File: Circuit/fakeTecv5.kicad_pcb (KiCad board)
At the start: 2 copper layers, 25.4 x 52.1 mm, 78 parts, among them J1 EXTRA, J11 FET1 3,3, J12 FET2 3,3, J13 FET3 3,3, J14 GPS Pins, J16 Encoder Pads, J37 SCL, J38 JST-SH-4, J39 SDA, J40 3.3V, J41 GND, J42 FET1, J43 FET2, J44 FET3, J45 GND, J46 3.3V, J47 GND, J48 GND, J49 GND, J5 I2C Oled screen, J50 3.3V, J51 GND, J52 GND, J6 FET1 Drain, J7 FET2 Drain, J8 FET3 Drain, J9 JST-PH-2, Q1 AO3400A, Q2 AO3400A, Q3 AO3400A, SW1 Reset, SW2 SW_Push, U1 XB8089D0, U2 HT-RA62, U3 nice!nano v2

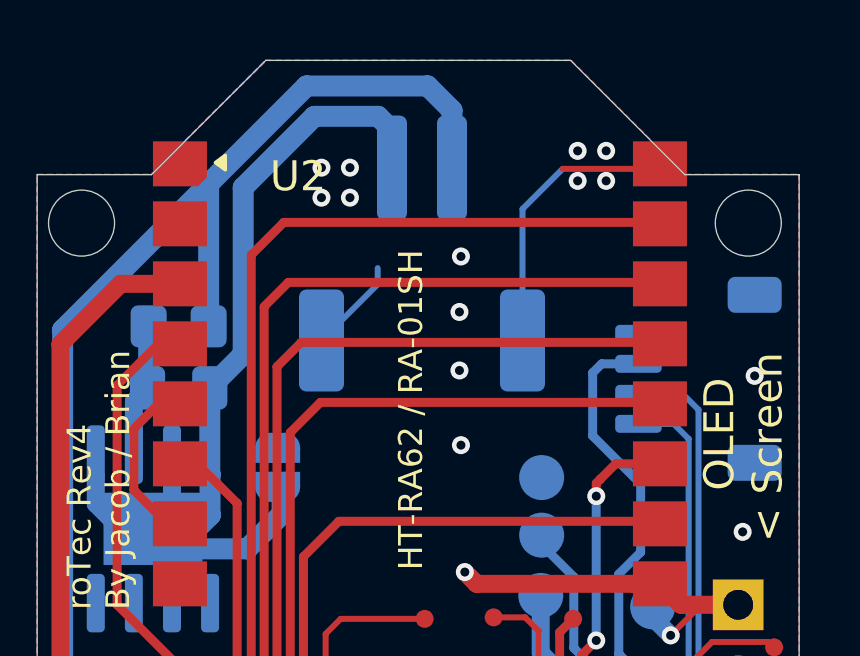
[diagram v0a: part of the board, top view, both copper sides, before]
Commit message: hw: modify power connector to support both JST GH and PH connector
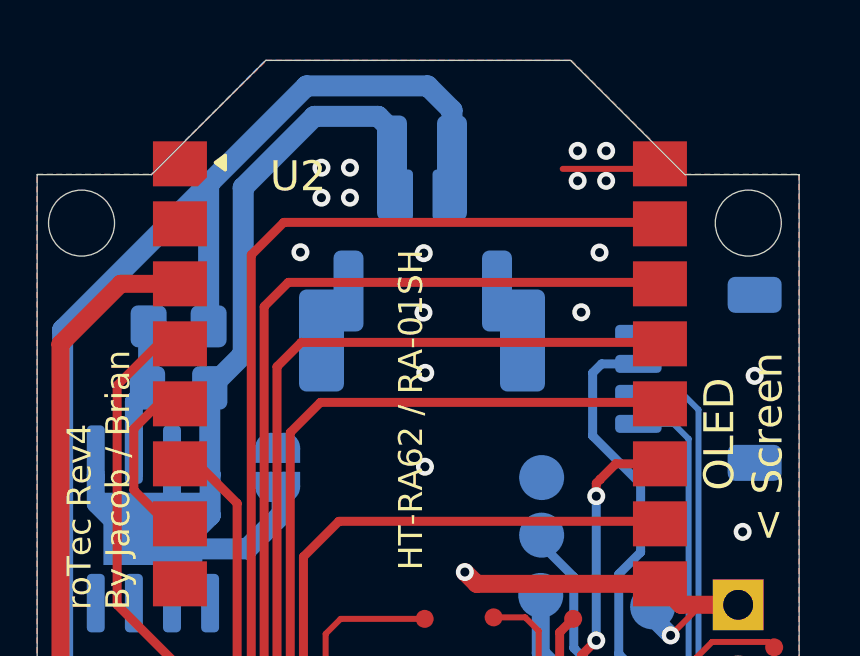
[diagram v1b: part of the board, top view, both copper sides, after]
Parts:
- J9: footprint Connector_JST:JST_PH_S2B-PH-SM4-TB_1x02-1MP_P2.00mm_Horizontal -> faketec:JST_PH_S2B-PH-SM4-TB_1x02-1MP_P2.00mm_Horizontal
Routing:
- net GND: track 133.1 -> 123.7 mm, vias 58 -> 61

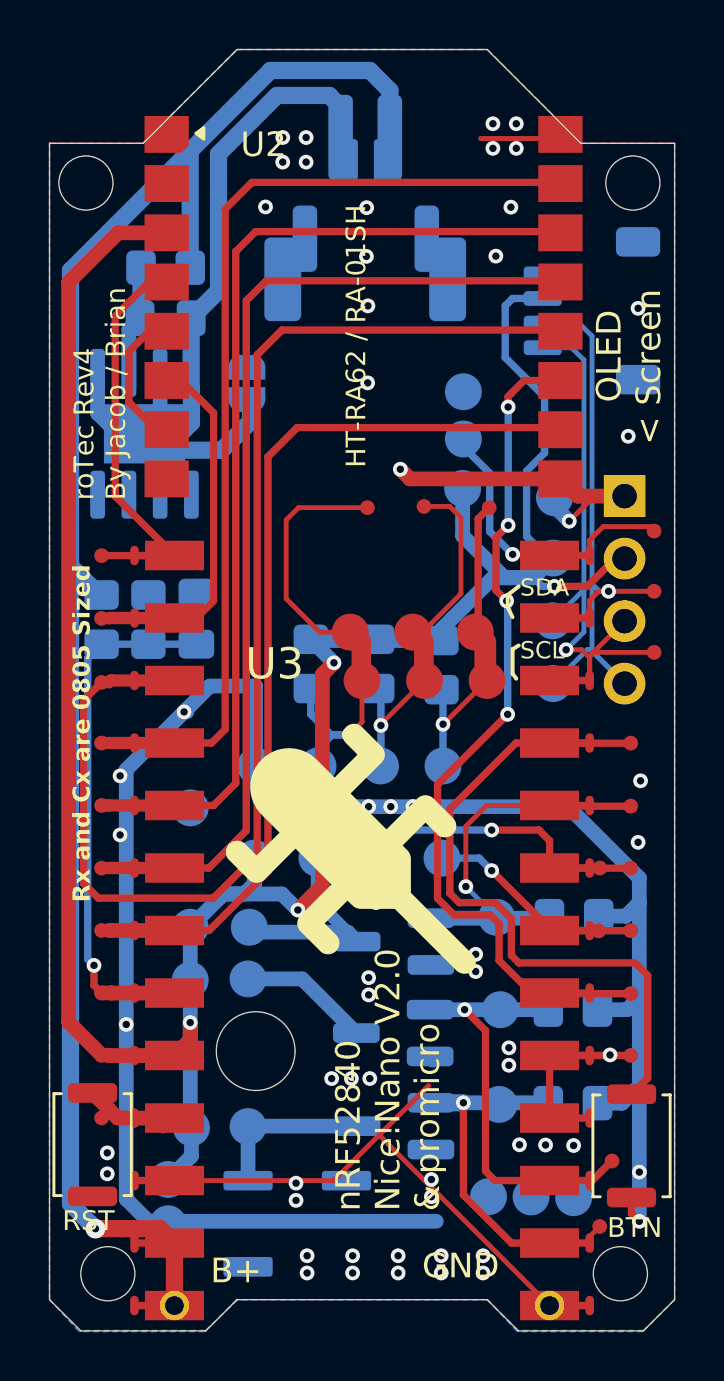
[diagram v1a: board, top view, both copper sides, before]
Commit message: hw: refactor spi routing. Make OLED screen pins friction fit
SPI is likely running under 50mHz mark so vias is not an issue and want to keep signal path small. Made careful note to keep all spi lines under the ground plane as much as possible.
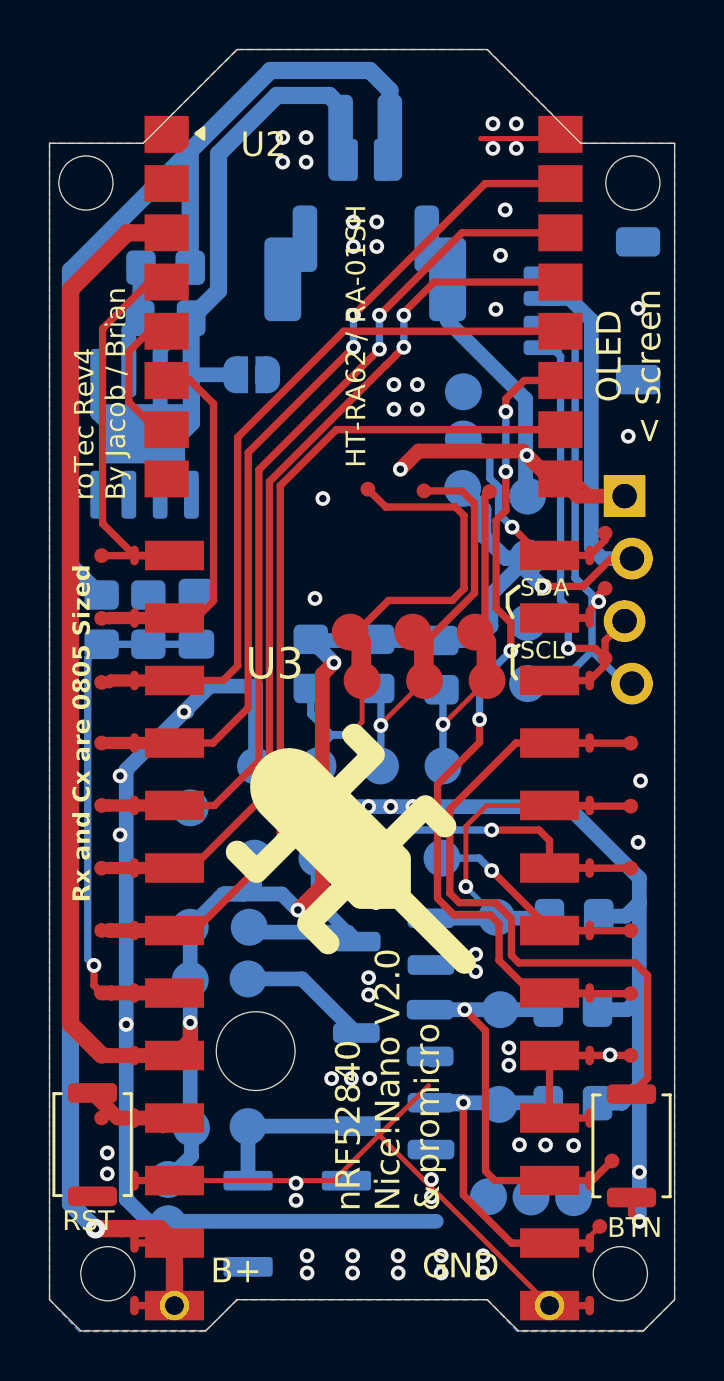
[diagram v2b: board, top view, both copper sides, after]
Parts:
- J5: footprint faketec:OLED_PinHeader_1x04_P2.54mm_Vertical -> faketec:OLED_PinHeader_1x04_P2.54mm_Vertical_Friction_Fit
- moved J25 2.00 mm to (121.5, 51.7)
- moved J24 1.99 mm to (121.5, 48.9)
- moved J23 1.99 mm to (121.5, 46.6)
- moved J41 1.09 mm to (118.3, 45.1)
- moved J3 0.75 mm to (111.8, 44.9)
- moved J22 0.65 mm to (116.8, 45.0)
- moved J2 0.63 mm to (114.1, 44.9)
- moved J37 0.58 mm to (118.8, 50.3)
- moved J40 0.54 mm to (118.8, 47.6)
- moved JP1 0.40 mm to (107.1, 40.2), turned to 180 degrees
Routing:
- net /SCK: track 52.5 -> 29.9 mm
- net GND: track 123.7 -> 132.5 mm, vias 61 -> 67
- net /CS: track 40.8 -> 34.7 mm, vias 0 -> 2
- net /MOSI: track 40.7 -> 35.8 mm, vias 0 -> 2
- net /MISO: track 40.8 -> 36.4 mm, vias 0 -> 2
- net /SCL: track 23.5 -> 19.4 mm
- net /ENC_PUSH: track 17.4 -> 20.9 mm
- net /SDA: track 27.3 -> 25.3 mm
- net /EXTRA: track 9.34 -> 7.40 mm
- net /ENC_A: track 14.9 -> 13.4 mm
- net /RST: track 16.3 -> 17.7 mm
- net -BATT: track 34.2 -> 32.9 mm
- net /BUSY: track 36.6 -> 35.3 mm

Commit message: hw: Thicker lines. All 0.2 lines converted to 0.3mm
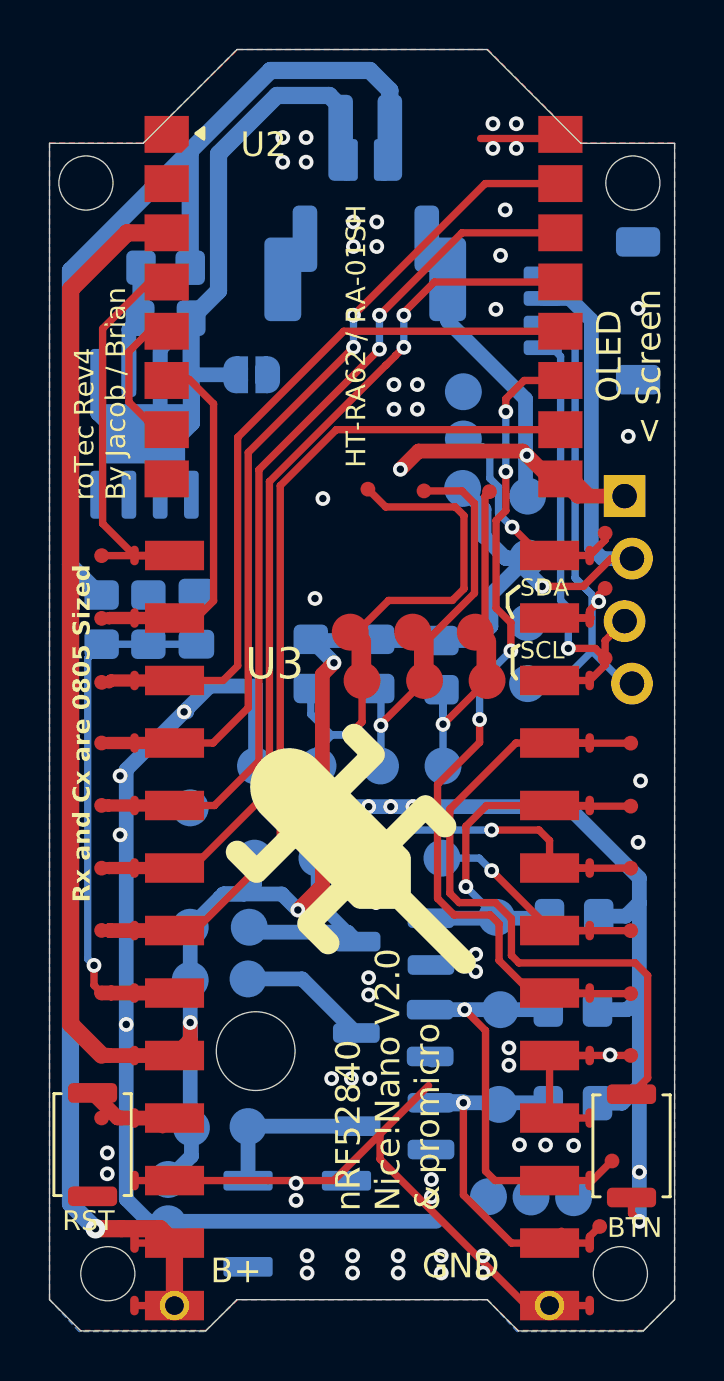
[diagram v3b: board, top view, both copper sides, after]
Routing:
- net GND: track 132.5 -> 133.1 mm
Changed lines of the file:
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@@
 		(start 103.65195 65.32401)
 		(end 103.96298 65.01298)
-		(width 0.2)
+		(width 0.3)
 		(layer "F.Cu")
 		(net 1)
@@
 		(start 103.96298 65.01298)
 		(end 103.96298 65.32401)
-		(width 0.2)
+		(width 0.3)
 		(layer "F.Cu")
 		(net 1)
@@
 	)
 	(segment
+		(start 119.20298 78.02401)
+		(end 118.26401 78.02401)
+		(width 0.3)
+		(layer "F.Cu")
+		(net 2)
+	)
+	(segment
 		(start 118.11 43.3)
 		(end 118.28 43.47)
@@
 		(start 121.01899 45.13101)
 		(end 122.25098 45.13101)
-		(width 0.2)
+		(width 0.3)
+		(layer "F.Cu")
+		(net 2)
+	)
+	(segment
+		(start 112.313 72.073)
+		(end 112.313 71.063)
+		(width 0.3)
 		(layer "F.Cu")
 		(net 2)
@@
 		(start 119.429058 30.6)
 		(end 116.4 30.6)
-		(width 0.2)
+		(width 0.3)
 		(layer "F.Cu")
 		(net 2)
@@
 		(start 107.75 72.94401)
 		(end 110.43199 72.94401)
-		(width 0.2)
+		(width 0.3)
+		(layer "F.Cu")
+		(net 2)
+	)
+	(segment
+		(start 118.26401 78.02401)
+		(end 112.313 72.073)
+		(width 0.3)
 		(layer "F.Cu")
 		(net 2)
@@
 	)
 	(segment
-		(start 112.313 71.13403)
-		(end 112.313 71.063)
-		(width 0.2)
-		(layer "F.Cu")
-		(net 2)
-	)
-	(segment
 		(start 119.41 67.86)
 		(end 122.51 67.86)
@@
 		(start 110.43199 72.94401)
 		(end 112.313 71.063)
-		(width 0.2)
+		(width 0.3)
 		(layer "F.Cu")
 		(net 2)
@@
 		(start 119.452024 30.622966)
 		(end 119.429058 30.6)
-		(width 0.2)
+		(width 0.3)
 		(layer "F.Cu")
 		(net 2)
@@
 		(start 103.96298 72.94401)
 		(end 107.75 72.94401)
-		(width 0.2)
+		(width 0.3)
 		(layer "F.Cu")
 		(net 2)
@@
 		(start 119.92798 44.04)
 		(end 121.01899 45.13101)
-		(width 0.2)
+		(width 0.3)
 		(layer "F.Cu")
 		(net 2)
@@
 		(start 112.313 71.063)
 		(end 114.288 69.088)
-		(width 0.2)
+		(width 0.3)
 		(layer "F.Cu")
 		(net 2)
@@
 	)
 	(segment
-		(start 119.20298 78.02401)
-		(end 112.313 71.13403)
-		(width 0.2)
-		(layer "F.Cu")
-		(net 2)
-	)
-	(segment
 		(start 122.25098 45.13101)
 		(end 120.34201 45.13101)
@@
 		(start 116.64599 57.70401)
 		(end 119.20298 57.70401)
-		(width 0.2)
+		(width 0.3)
 		(layer "F.Cu")
 		(net 17)
@@
 		(start 115.801 58.549)
 		(end 116.64599 57.70401)
-		(width 0.2)
+		(width 0.3)
 		(layer "F.Cu")
 		(net 17)
@@
 		(start 115.801 61)
 		(end 115.801 58.549)
-		(width 0.2)
+		(width 0.3)
 		(layer "F.Cu")
 		(net 17)
@@
 		(start 115.801 61)
 		(end 115.801 61.001)
-		(width 0.2)
+		(width 0.3)
 		(layer "B.Cu")
 		(net 17)
@@
 		(start 115.801 61.001)
 		(end 117.05 62.25)
-		(width 0.2)
+		(width 0.3)
 		(layer "B.Cu")
 		(net 17)
@@
 		(start 120.83298 75.21702)
 		(end 121.24 74.81)
-		(width 0.2)
+		(width 0.3)
 		(layer "F.Cu")
 		(net 21)
@@
 		(start 119.68699 75)
 		(end 119.20298 75.48401)
-		(width 0.2)
+		(width 0.3)
 		(layer "F.Cu")
 		(net 21)
@@
 		(start 120.83298 75.48401)
 		(end 120.83298 75.21702)
-		(width 0.2)
+		(width 0.3)
 		(layer "F.Cu")
 		(net 21)
@@
 		(start 120.89599 50.08401)
 		(end 120.83298 50.08401)
-		(width 0.2)
+		(width 0.3)
 		(layer "F.Cu")
 		(net 22)
@@
 		(start 122.25098 52.75101)
 		(end 122.65098 52.75101)
-		(width 0.2)
+		(width 0.3)
 		(layer "B.Cu")
 		(net 22)
@@
 		(start 119.283 60.16068)
 		(end 119.19967 60.24401)
-		(width 0.2)
+		(width 0.3)
 		(layer "F.Cu")
 		(net 24)
@@
 		(start 116.66298 52.62401)
 		(end 114.88699 54.4)
-		(width 0.2)
+		(width 0.3)
 		(layer "F.Cu")
 		(net 30)
@@
 		(start 114.88699 54.4)
 		(end 114.873 54.4)
-		(width 0.2)
+		(width 0.3)
 		(layer "F.Cu")
 		(net 30)
@@
 		(start 114.873 52.6)
 		(end 114.873 54.4)
-		(width 0.2)
+		(width 0.3)
 		(layer "B.Cu")
 		(net 30)
@@
 		(start 112.35 54.39699)
 		(end 114.12298 52.62401)
-		(width 0.2)
+		(width 0.3)
 		(layer "F.Cu")
 		(net 31)
@@
 		(start 112.35 54.45)
 		(end 112.35 54.39699)
-		(width 0.2)
+		(width 0.3)
 		(layer "F.Cu")
 		(net 31)
@@
 		(start 111.58298 54.30702)
 		(end 111.063 54.827)
-		(width 0.2)
+		(width 0.3)
 		(layer "F.Cu")
 		(net 32)
@@
 		(start 111.58298 52.62401)
 		(end 111.58298 54.30702)
-		(width 0.2)
+		(width 0.3)
 		(layer "F.Cu")
 		(net 32)
@@
 		(start 121.05 47.32699)
 		(end 120.83298 47.54401)
-		(width 0.2)
+		(width 0.3)
 		(layer "F.Cu")
 		(net 33)

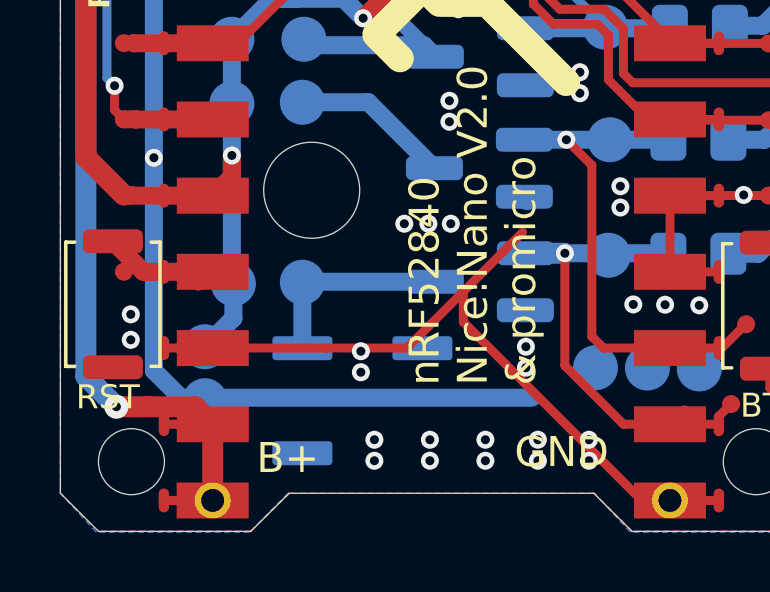
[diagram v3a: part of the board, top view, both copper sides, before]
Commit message: hw: Buzzer is wired incorrectly. Fixed wiring and updated schematic and pcb
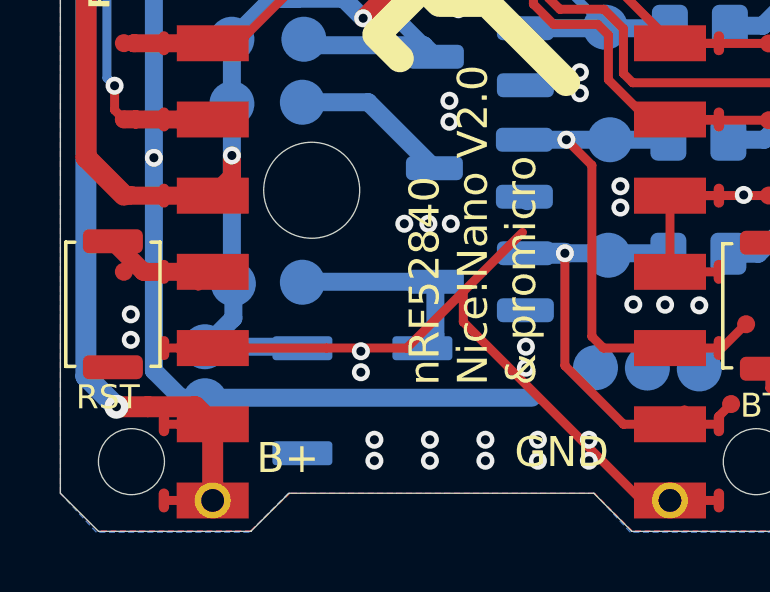
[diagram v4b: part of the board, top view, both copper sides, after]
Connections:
- BZ1 pad 1: /BUZZER -> +3.3V
- BZ1 pad 2: GND -> /BUZZER
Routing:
- net +3.3V: track 108.3 -> 111.6 mm
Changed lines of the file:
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@@
 			(layers "F.Cu" "F.Mask" "F.Paste")
 			(net 30 "/ENC_A")
-			(pinfunction "P1.07")
+			(pinfunction "P1.01")
 			(pintype "bidirectional")
 			(solder_mask_margin 0.1016)
@@
 			(layers "F.Cu")
 			(net 30 "/ENC_A")
-			(pinfunction "P1.07")
+			(pinfunction "P1.01")
 			(pintype "bidirectional")
 			(solder_mask_margin 0.1016)
@@
 			(layers "F.Cu" "F.Mask" "F.Paste")
 			(net 30 "/ENC_A")
-			(pinfunction "P1.07")
+			(pinfunction "P1.01")
 			(pintype "bidirectional")
 			(solder_mask_margin 0.1016)
@@
 			(layers "F.Cu" "F.Mask" "F.Paste")
 			(net 32 "/ENC_PUSH")
-			(pinfunction "P1.01")
+			(pinfunction "P1.07")
 			(pintype "bidirectional")
 			(solder_mask_margin 0.1016)
@@
 			(layers "F.Cu")
 			(net 32 "/ENC_PUSH")
-			(pinfunction "P1.01")
+			(pinfunction "P1.07")
 			(pintype "bidirectional")
 			(solder_mask_margin 0.1016)
@@
 			(layers "F.Cu" "F.Mask" "F.Paste")
 			(net 32 "/ENC_PUSH")
-			(pinfunction "P1.01")
+			(pinfunction "P1.07")
 			(pintype "bidirectional")
 			(solder_mask_margin 0.1016)
@@
 			(layers "B.Cu" "B.Mask" "B.Paste")
 			(roundrect_rratio 0.15)
-			(net 16 "/BUZZER")
+			(net 13 "+3.3V")
 			(pinfunction "+")
 			(pintype "passive")
@@
 			(layers "B.Cu" "B.Mask" "B.Paste")
 			(roundrect_rratio 0.15)
-			(net 2 "GND")
+			(net 16 "/BUZZER")
 			(pinfunction "-")
 			(pintype "passive")
@@
 	)
 	(segment
+		(start 103.7 72.9)
+		(end 106.9 72.9)
+		(width 0.6)
+		(layer "B.Cu")
+		(net 13)
+	)
+	(segment
 		(start 106.791 61.299)
 		(end 107.21 60.88)
@@
 	)
 	(segment
+		(start 106.9 72.9)
+		(end 106.95 72.95)
+		(width 0.6)
+		(layer "B.Cu")
+		(net 13)
+	)
+	(segment
 		(start 104.8 71.342)
 		(end 104.783 71.359)
@@
 	)
 	(segment
+		(start 111.383 70.734)
+		(end 111.383 72.517)
+		(width 0.6)
+		(layer "B.Cu")
+		(net 16)
+	)
+	(segment
 		(start 107.216 70.734)
 		(end 107 70.95)
@@
 	)
 	(segment
-		(start 106.95 72.9)
-		(end 106.95 70.75)
+		(start 111.383 72.517)
+		(end 110.95 72.95)
 		(width 0.6)
 		(layer "B.Cu")
